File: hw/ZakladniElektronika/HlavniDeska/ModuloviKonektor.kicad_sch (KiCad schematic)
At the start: 1 part, among them J4 Conn_01x07

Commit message: Nastin schematu
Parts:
- added R13 (x2): 4.7k, Resistor_SMD:R_0201_0603Metric, symbol Device:R
- added R23 (x3): 200, Resistor_SMD:R_0402_1005Metric, symbol Device:R
- added U2: TPD4E02B04DQA, Package_SON:USON-10_2.5x1.0mm_P0.5mm, symbol Power_Protection:TPD4E02B04DQA
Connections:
- net at J4.1 (Pin_1): now also R13.1, R23.1
- net 5V: now reaches J4.2 (Pin_2)
- net 5V: now also J4.6 (Pin_6), R13.2, R13.2, U2.5 (IO4)
- net GND: now reaches J4.3 (Pin_3)
- net GND: now also J4.5 (Pin_5), U2.3 (G), U2.8 (G)
- net at J4.4 (Pin_4): now also R23.1
- net at J4.7 (Pin_7): now also R13.1, R23.1
- new net INT: R23.2, U2.4 (IO3)
- new net USART-RX: R23.2, U2.1 (IO1)
- new net USART-TX: R23.2, U2.2 (IO2)
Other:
- moved on the sheet: J4

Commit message: WIP
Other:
- moved on the sheet: J4, R13, R23, U2

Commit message: Zavazbení zapínání
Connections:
- net 5V: no longer R13.2, R13.2
- new net 3V3: R13.2, R13.2
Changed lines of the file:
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@@
 (kicad_sch (version 20230121) (generator eeschema)
   (paper "A5")
-  (junction (at 124.46 38.1) (diameter 0) (color 0 0 0 0)
-  )
   (junction (at 83.82 50.8) (diameter 0) (color 0 0 0 0)
   )
@@
   )
   (junction (at 124.46 53.34) (diameter 0) (color 0 0 0 0)
-  )
-  (junction (at 119.38 38.1) (diameter 0) (color 0 0 0 0)
   )
   (junction (at 91.44 66.04) (diameter 0) (color 0 0 0 0)
@@
     (stroke (width 0) (type default))
   )
-  (wire (pts (xy 124.46 35.56) (xy 124.46 38.1))
-    (stroke (width 0) (type default))
-  )
-  (wire (pts (xy 124.46 38.1) (xy 119.38 38.1))
+  (wire (pts (xy 124.46 35.56) (xy 124.46 53.34))
     (stroke (width 0) (type default))
   )
@@
     (stroke (width 0) (type default))
   )
-  (wire (pts (xy 124.46 38.1) (xy 124.46 53.34))
-    (stroke (width 0) (type default))
-  )
   (wire (pts (xy 91.44 66.04) (xy 93.98 66.04))
     (stroke (width 0) (type default))
@@
     (stroke (width 0) (type default))
   )
-  (wire (pts (xy 119.38 38.1) (xy 109.22 38.1))
-    (stroke (width 0) (type default))
-  )
   (wire (pts (xy 101.6 66.04) (xy 119.38 66.04))
     (stroke (width 0) (type default))
   )
-  (wire (pts (xy 109.22 38.1) (xy 109.22 40.64))
+  (wire (pts (xy 109.22 36.83) (xy 109.22 40.64))
     (stroke (width 0) (type default))
   )
-  (wire (pts (xy 119.38 38.1) (xy 119.38 40.64))
+  (wire (pts (xy 119.38 36.83) (xy 119.38 40.64))
     (stroke (width 0) (type default))
   )
@@
     (effects (font (size 1.27 1.27)) (justify right))
   )
+  (hierarchical_label "3V3" (shape input) (at 109.22 36.83 90) (fields_autoplaced)
+    (effects (font (size 1.27 1.27)) (justify left))
+  )
   (hierarchical_label "GND" (shape input) (at 127 68.58 270) (fields_autoplaced)
     (effects (font (size 1.27 1.27)) (justify right))
   )
+  (hierarchical_label "3V3" (shape input) (at 119.38 36.83 90) (fields_autoplaced)
+    (effects (font (size 1.27 1.27)) (justify left))
+  )
   (symbol (lib_id "Connector_Generic:Conn_01x07") (at 134.62 58.42 0) (unit 1)

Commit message: USB_multiplexer a přehlednost
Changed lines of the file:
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@@
     (effects (font (size 1.27 1.27)) (justify left))
   )
-  (hierarchical_label "GND" (shape input) (at 88.9 86.36 270) (fields_autoplaced)
+  (hierarchical_label "GND" (shape passive) (at 127 68.58 270) (fields_autoplaced)
+    (effects (font (size 1.27 1.27)) (justify right))
+  )
+  (hierarchical_label "GND" (shape passive) (at 88.9 86.36 270) (fields_autoplaced)
     (effects (font (size 1.27 1.27)) (justify right))
   )
@@
     (effects (font (size 1.27 1.27)) (justify left))
   )
-  (hierarchical_label "GND" (shape input) (at 127 68.58 270) (fields_autoplaced)
-    (effects (font (size 1.27 1.27)) (justify right))
-  )
   (hierarchical_label "3V3" (shape input) (at 119.38 36.83 90) (fields_autoplaced)

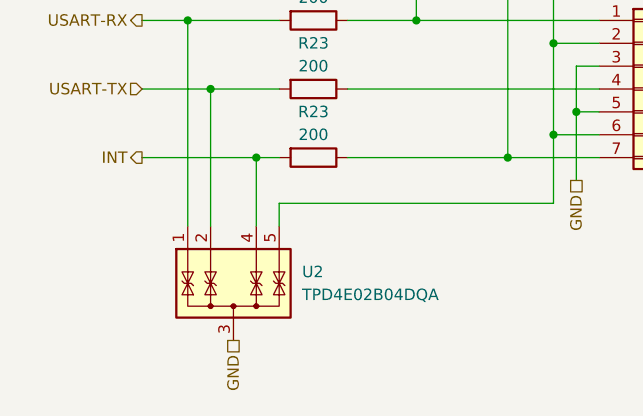
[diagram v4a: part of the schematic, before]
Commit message: Likvidace MiniUI jako samostatné desky a výběr všech komponent
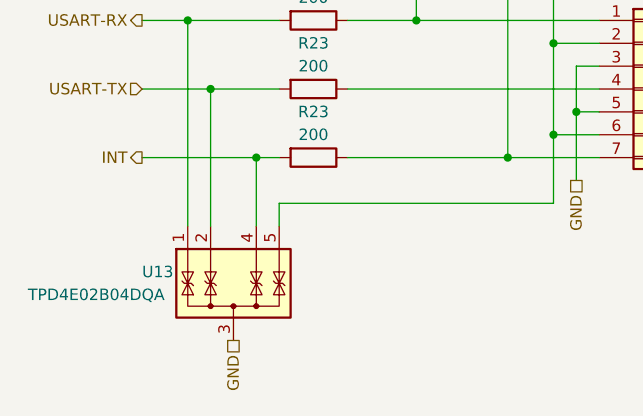
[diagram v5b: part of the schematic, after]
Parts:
- removed U2: TPD4E02B04DQA, Package_SON:USON-10_2.5x1.0mm_P0.5mm, symbol Power_Protection:TPD4E02B04DQA
- added U13: TPD4E02B04DQA, Package_SON:USON-10_2.5x1.0mm_P0.5mm, symbol RKL-Uncategorized:TPD4E02B04DQA
- J4: footprint (none) -> Connector_JST:JST_PH_S7B-PH-SM4-TB_1x07-1MP_P2.00mm_Horizontal; Basic/Extended (none) -> E; LCSC (none) -> C265453; info (none) -> další info viz: https://www.tme.eu/html/CZ/konektor-kabel-p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
- R13: footprint Resistor_SMD:R_0201_0603Metric -> Resistor_SMD:R_0402_1005Metric; Basic/Extended E -> B; LCSC C270346 -> C25900
- R23: Basic/Extended (none) -> B
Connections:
- net 5V: now also U13.5 (IO4)
- net GND: now also U13.3 (G), U13.8 (G)
- net INT: now also U13.4 (IO3)
- net USART-RX: now also U13.1 (IO1)
- net USART-TX: now also U13.2 (IO2)

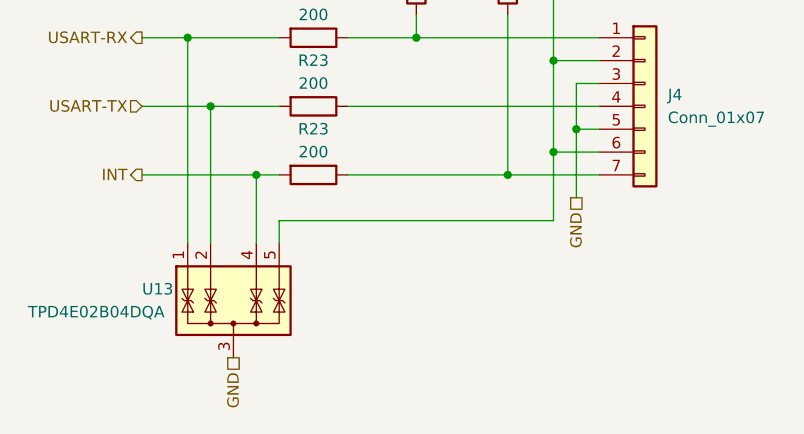
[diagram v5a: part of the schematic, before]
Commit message: Výmněna ochrany baterie
Předchozí ochranný čip JLCPCB nemělo na skladě
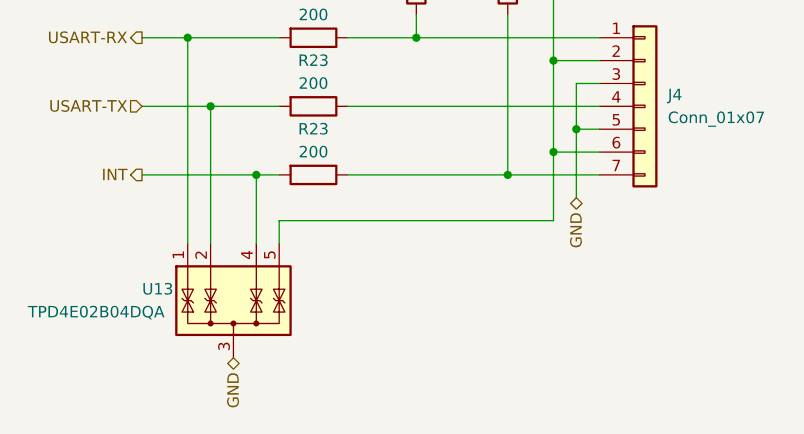
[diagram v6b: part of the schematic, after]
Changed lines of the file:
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@@
     (effects (font (size 1.27 1.27)) (justify left))
   )
-  (hierarchical_label "GND" (shape passive) (at 127 68.58 270) (fields_autoplaced)
+  (hierarchical_label "GND" (shape bidirectional) (at 127 68.58 270) (fields_autoplaced)
     (effects (font (size 1.27 1.27)) (justify right))
   )
-  (hierarchical_label "GND" (shape passive) (at 88.9 86.36 270) (fields_autoplaced)
+  (hierarchical_label "GND" (shape bidirectional) (at 88.9 86.36 270) (fields_autoplaced)
     (effects (font (size 1.27 1.27)) (justify right))
   )

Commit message: AHS-V1
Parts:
- U13: JLCPCB_CORRECTION (none) -> 0;0;-90
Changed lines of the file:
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@@
+      (effects (font (size 1.27 1.27)) hide)
+    )
+    (property "JLCPCB_CORRECTION" "0;0;-90" (at 88.9 76.2 0)
       (effects (font (size 1.27 1.27)) hide)
     )

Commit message: KiCad V8
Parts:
- renumbered R23 to R29, R23 to R30, R13 to R45, R13 to R48, R23 to R49, U13 to U5
